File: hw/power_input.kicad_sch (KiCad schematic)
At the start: 12 parts, among them Q101 100V N-ch, Q102 40V 5mOhm N-ch

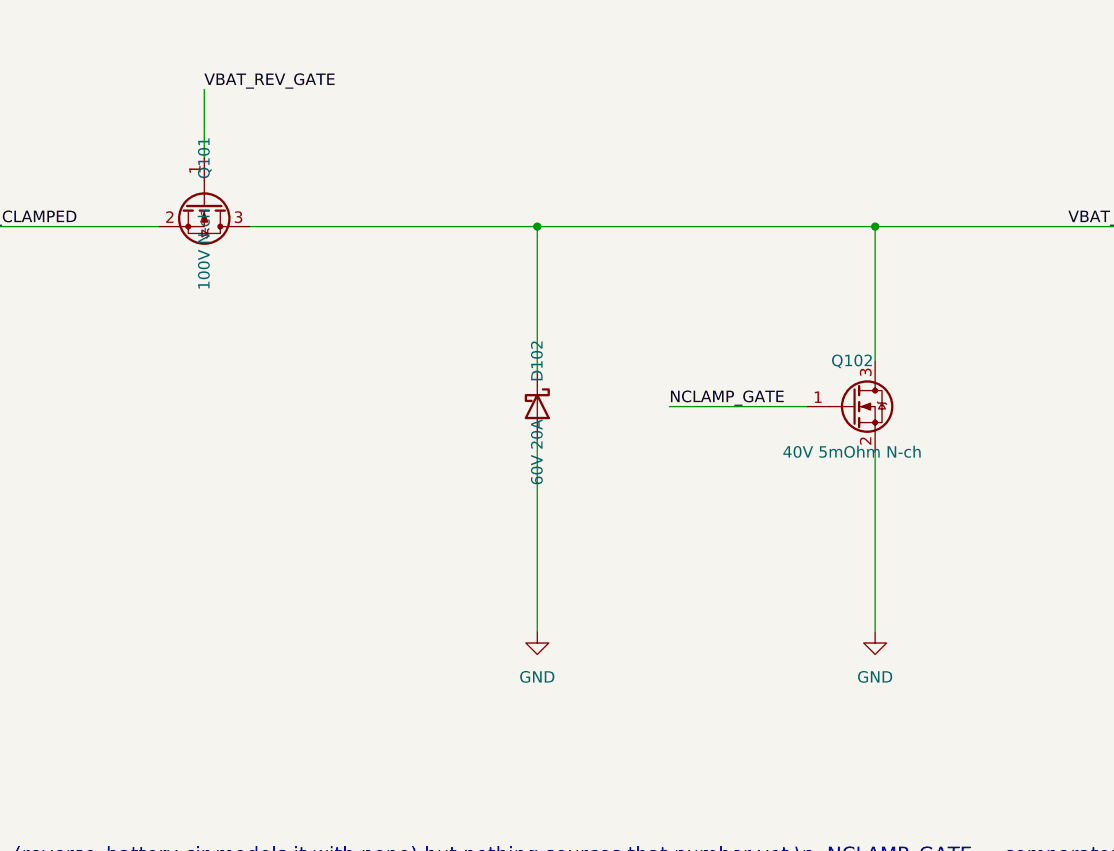
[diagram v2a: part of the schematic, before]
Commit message: Fix two under-rated clamp parts, and redraw the reverse FET as the block modelled it
Found while choosing power_input's clamp comparator. Two separate
findings, both the shape this project keeps turning up.

1. TWO PARTS UNDER-RATED FOR THE RAIL THEY SIT ON. NEG-CLAMP specified
   its FET at Vds >= 40 V and the backstop Schottky was 60 V. Both have
   a terminal on VBAT_PROT. Both were sized for the NEGATIVE pulses they
   exist to catch, and neither was checked against pulse 2a driving the
   SAME node to +73.3 V -- where the FET is 0.55x rated and the Schottky
   0.82x. The 40 V FET had zero margin on the 40 V load dump alone.

   transient_clamp.cir already carried "every part on VBAT_PROT must
   clear 73.3 V" -- as a principle, not a list, so nothing compared
   these two against it. It is now a TABLE in run_sim.py: every part
   with a terminal on the rail, its rating, and the margin, and a part
   below 1.09x fails. Twelve rows, each verified against the sheet that
   draws it rather than recalled. Both corrected parts are 100 V class;
   the table's own last claim records that both would have failed it.

2. THE REVERSE FET WAS DRAWN AT THE WRONG POLARITY. power_input drew an
   N-FET with an undriven controller gate. reverse_battery.cir has
   always modelled a P-FET -- "a P-FET held on by a controller that
   watches the polarity" -- and its switch closes on positive polarity.

   Choosing the controller showed why that matters. The node swings from
   +73.3 V (pulse 2a, after the TVS) to -47.8 V (pulse 1, the
   bidirectional TVS's negative clamp, bidirectional precisely so a
   reversed battery does not forward-bias it). No controller checked
   spans 121 V, both read from retrieved datasheets:

     LM74700-Q1   ANODE -65 V to +65 V  -- positive side short by 8.3 V
     LM5050-1-Q1  IN -0.3 V to +100 V   -- negative side short by
                  47.5 V, and IN draws 320 uA, so a series resistor to
                  protect it would corrupt its 20 mV dr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
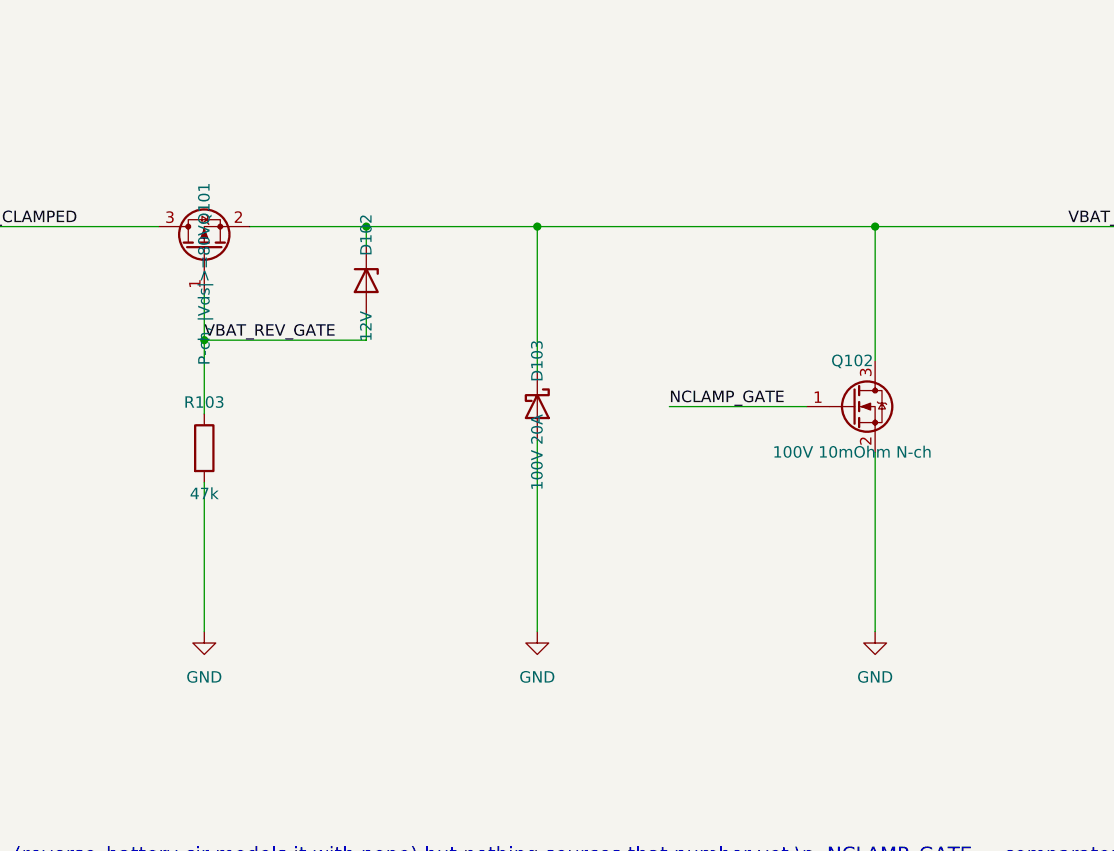
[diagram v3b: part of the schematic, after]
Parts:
- removed D102: 60V 20A, symbol Device:D_Schottky
- removed Q101: 100V N-ch, symbol Device:Q_NMOS_GSD
- added D102: 12V, symbol Device:D_Zener
- added D103: 100V 20A, symbol Device:D_Schottky
- added Q101: P-ch, |Vds|>=80V, symbol Device:Q_PMOS_GSD
- added R103: 47k, symbol Device:R
- Q102: value 40V 5mOhm N-ch -> 100V 10mOhm N-ch; Vds (none) -> 100 V class. It was 40 V until 22 Sep 2026 -- sized for the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
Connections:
- net GND: now also D103.2 (A), R103.2
- net VBAT_CLAMPED: now also Q101.3 (D)
- net VBAT_PROT: now also D102.1 (K), D103.1 (K), Q101.2 (S)
- net VBAT_REV_GATE: now also D102.2 (A), Q101.1 (G), R103.1
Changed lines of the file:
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@@
     (comment 2 "EMI filter values are emi_filter.cir element for element")
     (comment 3 "TVS and clamp: docs/bom_requirements.md tags TVS, NEG-CLAMP")
-    (comment 4 "Q1/Q2 gates are intentionally undriven -- see the note on the page")
+    (comment 4 "Q1 is a P-FET with a passive gate network; Q2's gate is undriven -- see the page")
   )
   (hierarchical_label "VBAT_IN" (shape input) (at 30.0 80.0 0)
@@
     (effects (font (size 1.27 1.27)) (justify left bottom))
   )
-  (symbol (lib_id "Device:Q_NMOS_GSD") (at 268.0 77.46 270) (unit 1)
-    (in_bom yes) (on_board yes) (fields_autoplaced)
-    (property "Reference" "Q101" (id 0) (at 268 72.38 0)
-      (effects (font (size 1.27 1.27)))
-    )
-    (property "Value" "100V N-ch" (id 1) (at 268 82.53999999999999 0)
-      (effects (font (size 1.27 1.27)))
-    )
-    (property "Footprint" "" (id 2) (at 268 77.46 0)
-      (effects (font (size 1.27 1.27)) hide)
-    )
-    (property "Datasheet" "~" (id 3) (at 268 77.46 0)
-      (effects (font (size 1.27 1.27)) hide)
-    )
-    (property "Source" "reverse_battery.cir; bom_requirements (reverse-battery FET)" (id 4) (at 268 77.46 0)
-      (effects (font (size 1.27 1.27)) hide)
-    )
-    (property "Note" "100 V class -- third revision, raised each time the clamp moved. Source to battery so the body diode blocks reverse current." (id 5) (at 268 77.46 0)
-      (effects (font (size 1.27 1.27)) hide)
-    )
-    (property "Rds_on" "8 mOhm modelled" (id 6) (at 268 77.46 0)
+  (symbol (lib_id "Device:Q_PMOS_GSD") (at 268.0 82.54 90) (unit 1)
+    (in_bom yes) (on_board yes) (fields_autoplaced)
+    (property "Reference" "Q101" (id 0) (at 268 77.46000000000001 0)
+      (effects (font (size 1.27 1.27)))
+    )
+    (property "Value" "P-ch, |Vds|>=80V" (id 1) (at 268 87.62 0)
+      (effects (font (size 1.27 1.27)))
+    )
+    (property "Footprint" "" (id 2) (at 268 82.54 0)
+      (effects (font (size 1.27 1.27)) hide)
+    )
+    (property "Datasheet" "~" (id 3) (at 268 82.54 0)
+      (effects (font (size 1.27 1.27)) hide)
+    )
+    (property "Source" "reverse_battery.cir path B -- modelled as a P-FET all along" (id 4) (at 268 82.54 0)
+      (effects (font (size 1.27 1.27)) hide)
+    )
+    (property "Note" "Drain to battery, source to load. |Vds| worst case is 47.8 V, blocking pulse 1 with the load side clamped near zero; 80 V class anyway, by the board's own rail rule." (id 5) (at 268 82.54 0)
+      (effects (font (size 1.27 1.27)) hide)
+    )
+    (property "Rds_on" "<=40 mOhm at Vgs = -4.5 V: 0.2 V at 5 A against reverse_battery.cir's 0.3 V requirement, and specified at -4.5 V because at a 6 V cranking dip that is all the gate gets" (id 6) (at 268 82.54 0)
       (effects (font (size 1.27 1.27)) hide)
     )
@@
     (stroke (width 0) (type default))
   )
-  (wire (pts (xy 268.0 72.38) (xy 268.0 64.76))
-    (stroke (width 0) (type default))
-  )
-  (label "VBAT_REV_GATE" (at 268.0 64.76 0)
+  (wire (pts (xy 268.0 87.62) (xy 268.0 92.62))
+    (stroke (width 0) (type default))
+  )
+  (label "VBAT_REV_GATE" (at 268.0 92.62 180)
     (effects (font (size 1.27 1.27)) (justify left bottom))
   )
-  (wire (pts (xy 273.08 80.0) (xy 305.0 80.0))
+  (symbol (lib_id "Device:R") (at 268.0 104.62 0) (unit 1)
+    (in_bom yes) (on_board yes) (fields_autoplaced)
+    (property "Reference" "R103" (id 0) (at 268 99.54 0)
+      (effects (font (size 1.27 1.27)))
+    )
+    (property "Value" "47k" (id 1) (at 268 109.7 0)
+      (effects (font (size 1.27 1.27)))
+    )
+    (property "Footprint" "" (id 2) (at 268 104.62 0)
+      (effects (font (size 1.27 1.27)) hide)
+    )
+    (property "Datasheet" "~" (id 3) (at 268 104.62 0)
+      (effects (font (size 1.27 1.27)) hide)
+    )
+    (property "Note" "Gate to ground. Carries (73.3 - 12) / 47k = 1.3 mA through pulse 2a, 32 uA at 13.5 V. With Ciss it also sets the turn-off time when the load side is pulled to zero -- tens of microseconds, which is why the negative clamp is sized for this FET staying ON through a whole pulse." (id 4) (at 268 104.62 0)
+      (effects (font (size 1.27 1.27)) hide)
+    )
+  )
+  (wire (pts (xy 268.0 92.62) (xy 268.0 100.81))
+    (stroke (width 0) (type default))
+  )
+  (wire (pts (xy 268.0 108.43) (xy 268.0 125.0))
+    (stroke (width 0) (type default))
+  )
+  (symbol (lib_id "power:GND") (at 268.0 125.0 0) (unit 1)
+    (in_bom yes) (on_board yes) (fields_autoplaced)
+    (property "Reference" "#PWR105" (id 0) (at 268 119.92 0)
+      (effects (font (size 1.27 1.27)) hide)
+    )
+    (property "Value" "GND" (id 1) (at 268 130.08 0)
+      (effects (font (size 1.27 1.27)))
+    )
+    (property "Footprint" "" (id 2) (at 268 125.0 0)
+      (effects (font (size 1.27 1.27)) hide)
+    )
+    (property "Datasheet" "~" (id 3) (at 268 125.0 0)
+      (effects (font (size 1.27 1.27)) hide)
+    )
+  )
+  (junction (at 268.0 92.62) (diameter 0) (color 0 0 0 0)
+  )
+  (symbol (lib_id "Device:D_Zener") (at 286.0 86.0 270) (unit 1)
+    (in_bom yes) (on_board yes) (fields_autoplaced)
+    (property "Reference" "D102" (id 0) (at 286.0 80.92 0)
+      (effects (font (size 1.27 1.27)))
+    )
+    (property "Value" "12V" (id 1) (at 286.0 91.08 0)
+      (effects (font (size 1.27 1.27)))
+    )
+    (property "Footprint" "" (id 2) (at 286.0 86.0 0)
+      (effects (font (size 1.27 1.27)) hide)
+    )
+    (property "Datasheet" "~" (id 3) (at 286.0 86.0 0)
+      (effects (font (size 1.27 1.27)) hide)
+    )
+    (property "Note" "Cathode to SOURCE, anode to GATE: clamps Vgs at -12 V, inside a P-FET's +/-20 V rating, whatever the rail does." (id 4) (at 286.0 86.0 0)
+      (effects (font (size 1.27 1.27)) hide)
+    )
+  )
+  (wire (pts (xy 286.0 89.81) (xy 286.0 92.62))
+    (stroke (width 0) (type default))
+  )
+  (wire (pts (xy 286.0 92.62) (xy 268.0 92.62))
+    (stroke (width 0) (type default))
+  )
+  (wire (pts (xy 273.08 80.0) (xy 286.0 80.0))
+    (stroke (width 0) (type default))
+  )
+  (wire (pts (xy 286.0 80.0) (xy 286.0 82.19))
+    (stroke (width 0) (type default))
+  )
+  (junction (at 286.0 80.0) (diameter 0) (color 0 0 0 0)
+  )
+  (wire (pts (xy 286.0 80.0) (xy 305.0 80.0))
     (stroke (width 0) (type default))
   )
   (symbol (lib_id "Device:D_Schottky") (at 305.0 100.0 270) (unit 1)
     (in_bom yes) (on_board yes) (fields_autoplaced)
-    (property "Reference" "D102" (id 0) (at 305 94.92 0)
-      (effects (font (size 1.27 1.27)))
-    )
-    (property "Value" "60V 20A" (id 1) (at 305 105.08 0)
+    (property "Reference" "D103" (id 0) (at 305 94.92 0)
+      (effects (font (size 1.27 1.27)))
+    )
+    (property "Value" "100V 20A" (id 1) (at 305 105.08 0)
       (effects (font (size 1.27 1.27)))
     )
@@
       (effects (font (size 1.27 1.27)) hide)
     )
-    (property "Ipk" "13.58 A measured" (id 6) (at 305 100.0 0)
+    (property "Vr" "100 V class. It was 60 V until 22 Sep 2026: rated for the negative pulse it exists to catch, and not for pulse 2a pushing the SAME node to +73.3 V in reverse." (id 6) (at 305 100.0 0)
+      (effects (font (size 1.27 1.27)) hide)
+    )
+    (property "Ipk" "13.58 A measured" (id 7) (at 305 100.0 0)
       (effects (font (size 1.27 1.27)) hide)
     )
@@
   (symbol (lib_id "power:GND") (at 305.0 125.0 0) (unit 1)
     (in_bom yes) (on_board yes) (fields_autoplaced)
-    (property "Reference" "#PWR105" (id 0) (at 305 119.92 0)
+    (property "Reference" "#PWR106" (id 0) (at 305 119.92 0)
       (effects (font (size 1.27 1.27)) hide)
     )
@@
       (effects (font (size 1.27 1.27)))
     )
-    (property "Value" "40V 5mOhm N-ch" (id 1) (at 340 105.08 0)
+    (property "Value" "100V 10mOhm N-ch" (id 1) (at 340 105.08 0)
       (effects (font (size 1.27 1.27)))
     )
@@
       (effects (font (size 1.27 1.27)) hide)
     )
-    (property "Rds_on" "10 mOhm max at Vgs=4.5 V" (id 6) (at 340 100.0 0)
+    (property "Vds" "100 V class. It was 40 V until 22 Sep 2026 -- sized for the negative pulses it clamps, with its drain on a node pulse 2a drives to +73.3 V. 40 V had zero margin on the load dump alone." (id 6) (at 340 100.0 0)
+      (effects (font (size 1.27 1.27)) hide)
+    )
+    (property "Rds_on" "10 mOhm max at Vgs=4.5 V" (id 7) (at 340 100.0 0)
       (effects (font (size 1.27 1.27)) hide)
     )
@@
   (symbol (lib_id "power:GND") (at 342.54 125.0 0) (unit 1)
     (in_bom yes) (on_board yes) (fields_autoplaced)
-    (property "Reference" "#PWR106" (id 0) (at 342.54 119.92 0)
-      (effects (font (size 1.27 1.27)) hide)
-    )
+    (property "Reference" "#PWR107" (id 0) (at 342.54 119.92 0)
+      (effects (font (size 1.27 1.27)) hide)
+    )

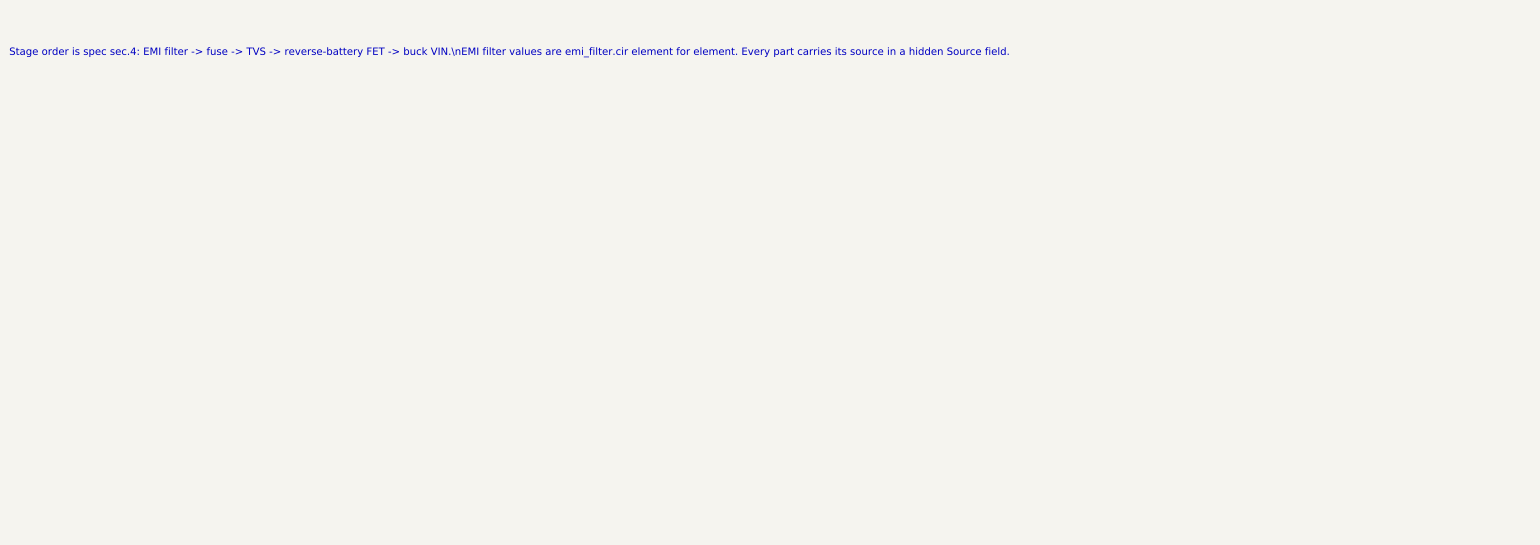
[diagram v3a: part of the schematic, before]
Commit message: Choose the negative clamp's control, and fix the latch a passing check hid
TLV3201-Q1 comparator into a UCC27517A-Q1 driver, both from retrieved
datasheets. The comparator's 52 mA would take about half a microsecond
to charge the clamp FET's gate; the driver's 4 A takes nanoseconds.

THE CLAMP LATCHED, AND run_sim.py SAID IT WAS RESOLVED. The model engaged
the active clamp near VIN = +0.08 V and released it only above +0.12 V.
At the end of every negative pulse the source returns to +13.5 V and
drives current back through the still-on clamp: 1.35 A through 5 mOhm is
6.7 mV, never reaching the release threshold. So the clamp stayed on and
shorted the source for the rest of the run -- clamped VIN sat at
0.0067 V while the Schottky-only branch recovered to 11.25 V. The check
measured only the clamp branch's MINIMUM. A recovery check, added first
and seen to fail on both pulse 1 and pulse 3a, is now permanent. With a
real battery in place of the test generator's 10 ohm, that is a dead
short after the first negative pulse.

The clamp is a low-side ideal diode -- anode ground, cathode VIN -- and
now engages below -100 mV and releases above -6.8 mV. Both thresholds sit
below ground, and a single-supply comparator has no negative reference,
so the sense node is lifted: 10k from VIN and 499k from 5V_MAIN put it at
0.9804 x VIN + 98.2 mV. Reference: 10k to ground, 536k from the output.
The drawn network and the model's thresholds are now tied by arithmetic
checks. 523k, the first value, put the worst-case release at +0.5 mV --
above zero, and the claim that said otherwise was reworded by moving the
resistor rather than the words.

THE WINDOW BEFORE IT ENGAGES IS A NUMBER NOW, AND IT IS INSIDE THE
RATING. With ~100 ns of delay (50 + 23 ns max, plus gate charge) VIN
crosses -100 mV, keeps falling ~90 ns, and bottoms at -0.177 V -- 1.70x
inside the LM5164's -0.3 V. The previous -0.068 V was optimistic by 2.6x:
at the default timestep ngspice committed the hysteretic switch on a
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
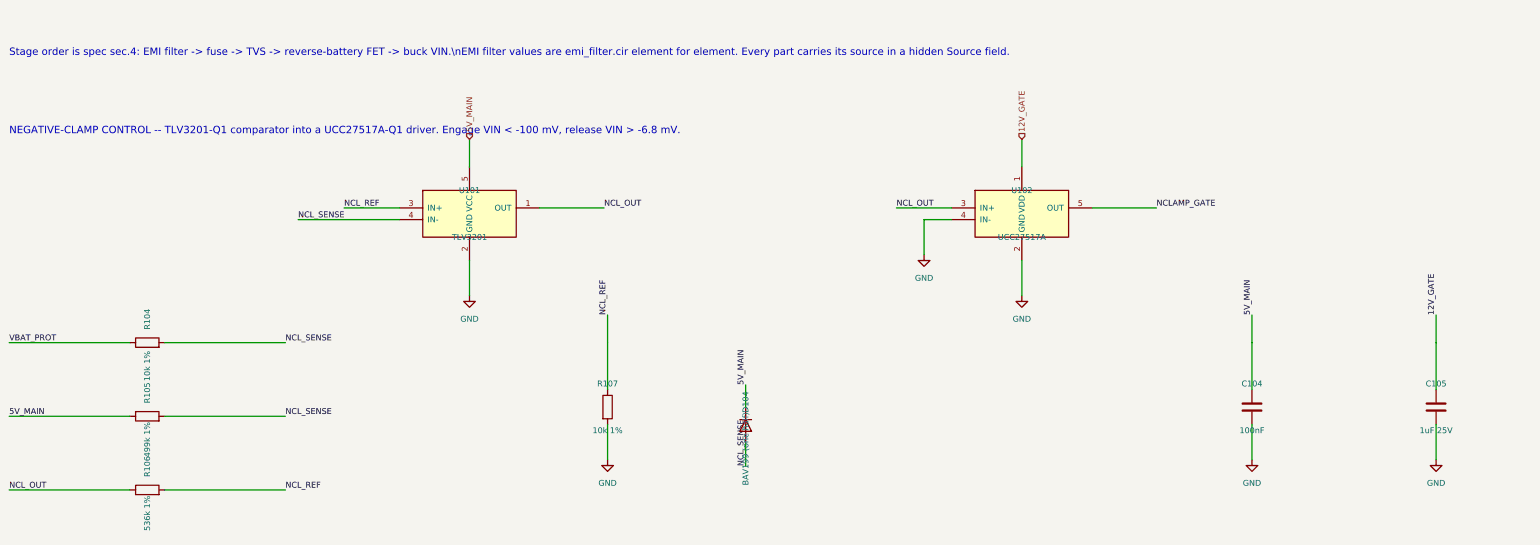
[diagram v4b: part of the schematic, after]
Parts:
- added C104: 100nF, symbol Device:C
- added C105: 1uF 25V, symbol Device:C
- added D104: BAV199 (one half), symbol Device:D
- added R104, R107: 10k 1%, symbol Device:R
- added R105: 499k 1%, symbol Device:R
- added R106: 536k 1%, symbol Device:R
- added U101: TLV3201, Package_TO_SOT_SMD:SOT-353_SC-70-5, symbol ecu25kva:TLV3201
- added U102: UCC27517A, Package_TO_SOT_SMD:SOT-23-5, symbol ecu25kva:UCC27517A
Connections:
- net GND: now also C104.2, C105.2, R107.2, U101.2 (GND), U102.2 (GND), U102.4 (IN-)
- net NCLAMP_GATE: now also U102.5 (OUT)
- net VBAT_PROT: now also R104.1
- new net 12V_GATE: C105.1, U102.1 (VDD)
- new net 5V_MAIN: C104.1, D104.1 (K), R105.1, U101.5 (VCC)
- new net NCL_OUT: R106.1, U101.1 (OUT), U102.3 (IN+)
- new net NCL_REF: R106.2, R107.1, U101.3 (IN+)
- new net NCL_SENSE: D104.2 (A), R104.2, R105.2, U101.4 (IN-)
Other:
- note added: "NEGATIVE-CLAMP CONTROL -- TLV3201-Q1 comparator into a UCC27517A-Q1 driver. Engage VIN < -100 mV, release VIN > -6.8 mV."
